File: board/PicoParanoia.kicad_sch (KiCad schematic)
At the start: 61 parts, among them J1 RCAJack, J2 Barrel_Jack_Switch, J3 Conn_01x04_Pin, J4 DE9_Plug, P1 Mini-DIN_6pins_ver4, Q1 2N3904, Q2 2N3904, Q3 2N3904, Q4 2N3904, U1 MicroSD_SPI_CD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

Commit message: JLCPCB order
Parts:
- removed H1, H2, H3, H4: MountingHole, MountingHole:MountingHole_3.2mm_M3, symbol Mechanical:MountingHole
- added C16: 100 nF, Capacitor_THT:C_Disc_D5.0mm_W2.5mm_P5.00mm, symbol Device:C_Small
- added H1, H2, H3, H4: MountingHole_Pad, MountingHole:MountingHole_3.2mm_M3_Pad, symbol Mechanical:MountingHole_Pad
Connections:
- net +5V: now also C16.1
- net GND: now also C16.2, H1.1, H2.1, H3.1, H4.1
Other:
- moved on the sheet: C5, R12

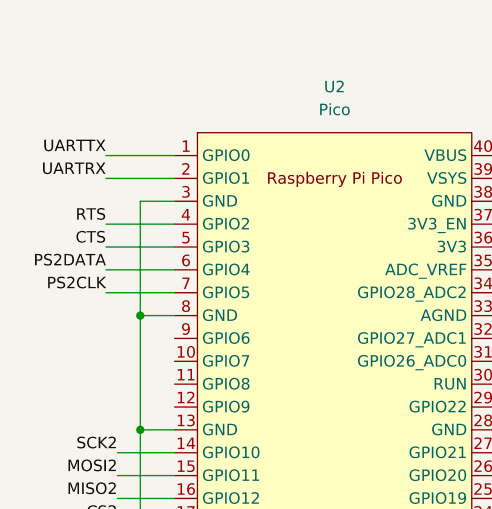
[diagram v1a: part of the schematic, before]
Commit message: Swapped cipher and plaintext cards
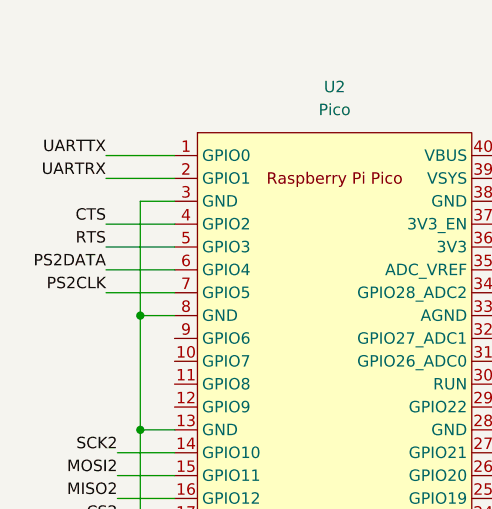
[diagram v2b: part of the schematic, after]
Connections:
- net CTS: now also U2.4 (GPIO2); no longer U2.5 (GPIO3)
- net RTS: now also U2.5 (GPIO3); no longer U2.4 (GPIO2)
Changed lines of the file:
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@@
     (effects (font (size 1.27 1.27)) (justify left bottom))
   )
-  (label "CTS" (at 21.59 44.45 180) (fields_autoplaced)
+  (label "CTS" (at 21.59 41.91 180) (fields_autoplaced)
     (effects (font (size 1.27 1.27)) (justify right bottom))
   )
@@
     (effects (font (size 1.27 1.27)) (justify right bottom))
   )
-  (label "RTS" (at 21.59 41.91 180) (fields_autoplaced)
+  (label "RTS" (at 21.59 44.45 180) (fields_autoplaced)
     (effects (font (size 1.27 1.27)) (justify right bottom))
   )
